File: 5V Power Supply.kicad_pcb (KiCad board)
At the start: 2 copper layers, 28.3 x 18 mm, 17 parts, among them Q1 CSD13202Q2, U1 TPS61287RZPR

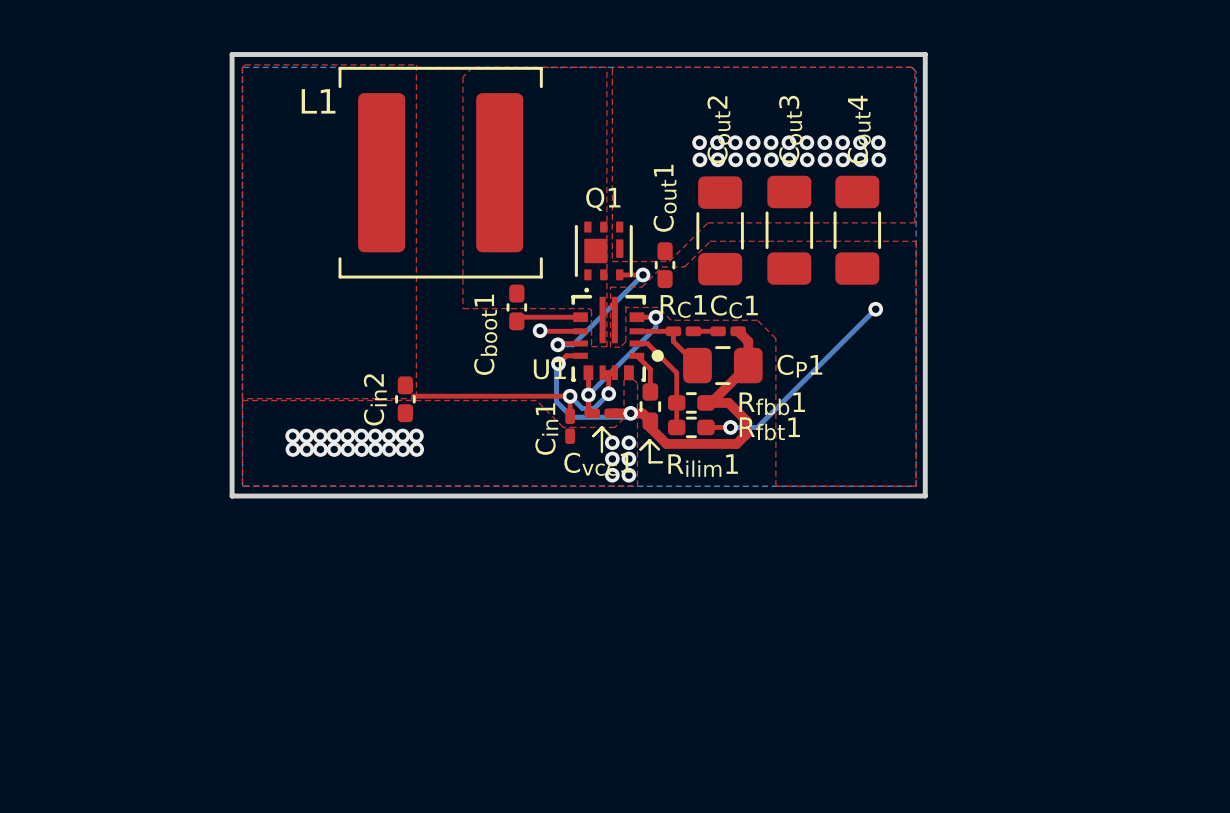
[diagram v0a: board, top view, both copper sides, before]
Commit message: feat: Mounting holes, power connectors
Added 2.54 mm ID mounting holes and 4 power connectors. Phoenix Contact spring loaded, good to 16 A, 14-26 AWG wire. 1x on power input from batt, 3x on +5V output.
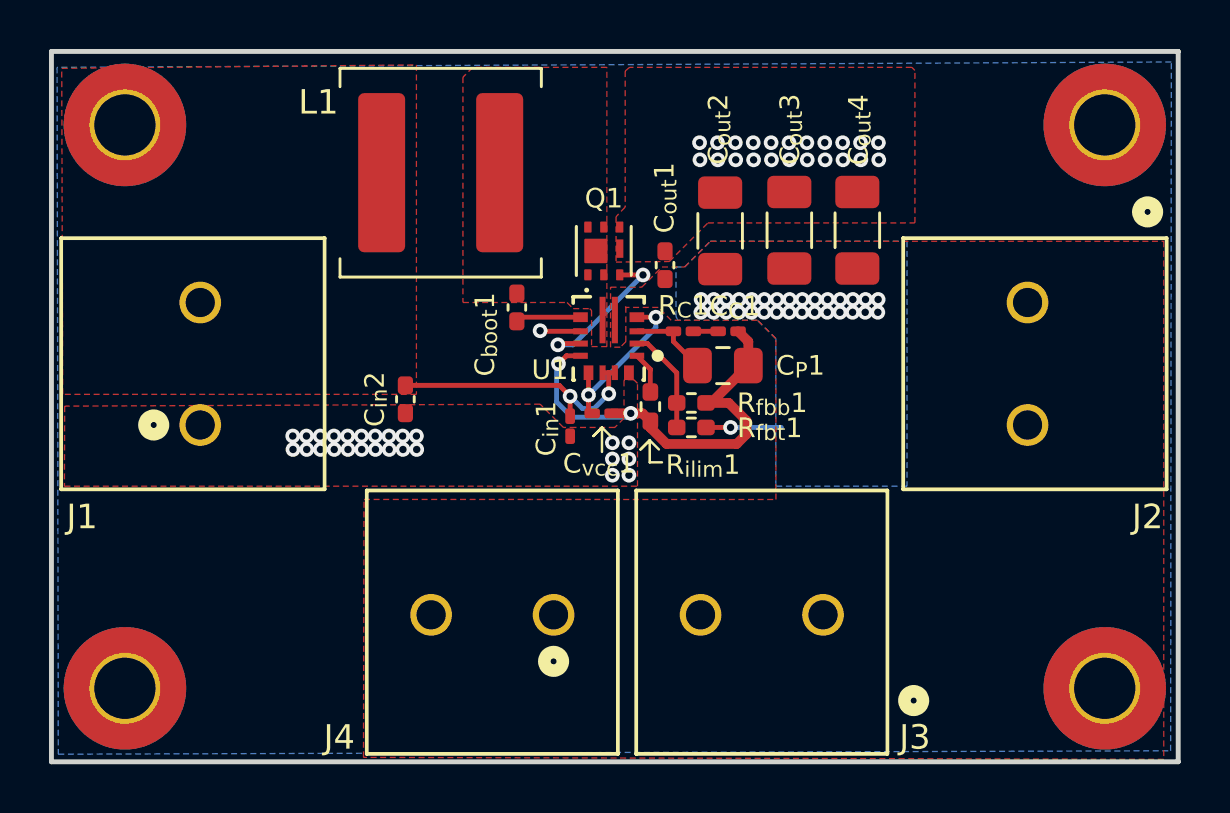
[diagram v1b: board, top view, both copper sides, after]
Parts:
- added J1: 1792863, 1792863:CONN_1792863_PXC, F.Cu at (60.1, 55.0)
- added J2: 1792863, 1792863:CONN_1792863_PXC, F.Cu at (93.8, 50.0)
- added J3: 1792863, 1792863:CONN_1792863_PXC, F.Cu at (85.5, 62.8)
- added J4: 1792863, 1792863:CONN_1792863_PXC, F.Cu at (74.5, 62.8)
- added REF**: MountingHole_2.5mm_Pad_TopBottom, MountingHole:MountingHole_2.5mm_Pad_TopBottom, F.Cu at (97.0, 65.8)
- added REF**: MountingHole_2.5mm_Pad_TopBottom, MountingHole:MountingHole_2.5mm_Pad_TopBottom, F.Cu at (97.0, 42.8)
- added REF**: MountingHole_2.5mm_Pad_TopBottom, MountingHole:MountingHole_2.5mm_Pad_TopBottom, F.Cu at (57.0, 65.8)
- added REF**: MountingHole_2.5mm_Pad_TopBottom, MountingHole:MountingHole_2.5mm_Pad_TopBottom, F.Cu at (57.0, 42.8)
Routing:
- net +5VDC: track 9.03 -> 3.08 mm, vias 2 -> 31
- net Vbat: track 10.6 -> 11.1 mm
- added copper zone on B.Cu, net +5VDC
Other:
- board size 28.3 x 18 mm -> 46 x 29 mm

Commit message: Added test points, silkscreening.
Need to consider input connector. Only rated to 16 A, but at lowest input voltage and highest output current need 18 A on input.
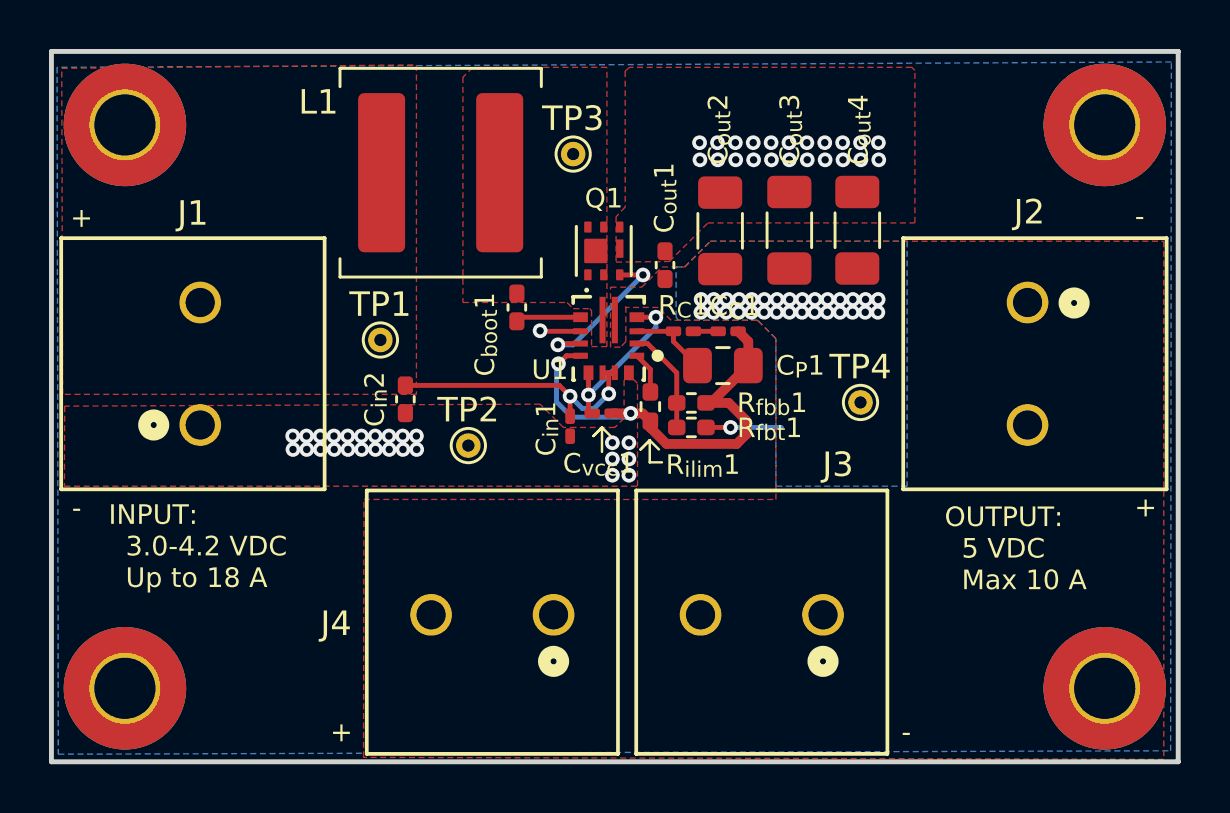
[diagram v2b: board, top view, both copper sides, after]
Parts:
- added TP1: TestPoint, TestPoint:TestPoint_THTPad_D1.0mm_Drill0.5mm, F.Cu at (67.4, 51.5)
- added TP2: TestPoint, TestPoint:TestPoint_THTPad_D1.0mm_Drill0.5mm, F.Cu at (71.0, 55.8)
- added TP3: TestPoint, TestPoint:TestPoint_THTPad_D1.0mm_Drill0.5mm, F.Cu at (75.3, 43.9)
- added TP4: TestPoint, TestPoint:TestPoint_THTPad_D1.0mm_Drill0.5mm, F.Cu at (87.0, 54.1)
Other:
- board text added: "+"
- board text added: "-"
- board text added: "INPUT: 3.0-4.2 VDC Up to 18 A"
- board text added: "OUTPUT: 5 VDC Max 10 A"

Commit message: Updated footprints
* Some of the footprints didn't match the size of the part picked for this project.
* Two of the capacitors were swapped.
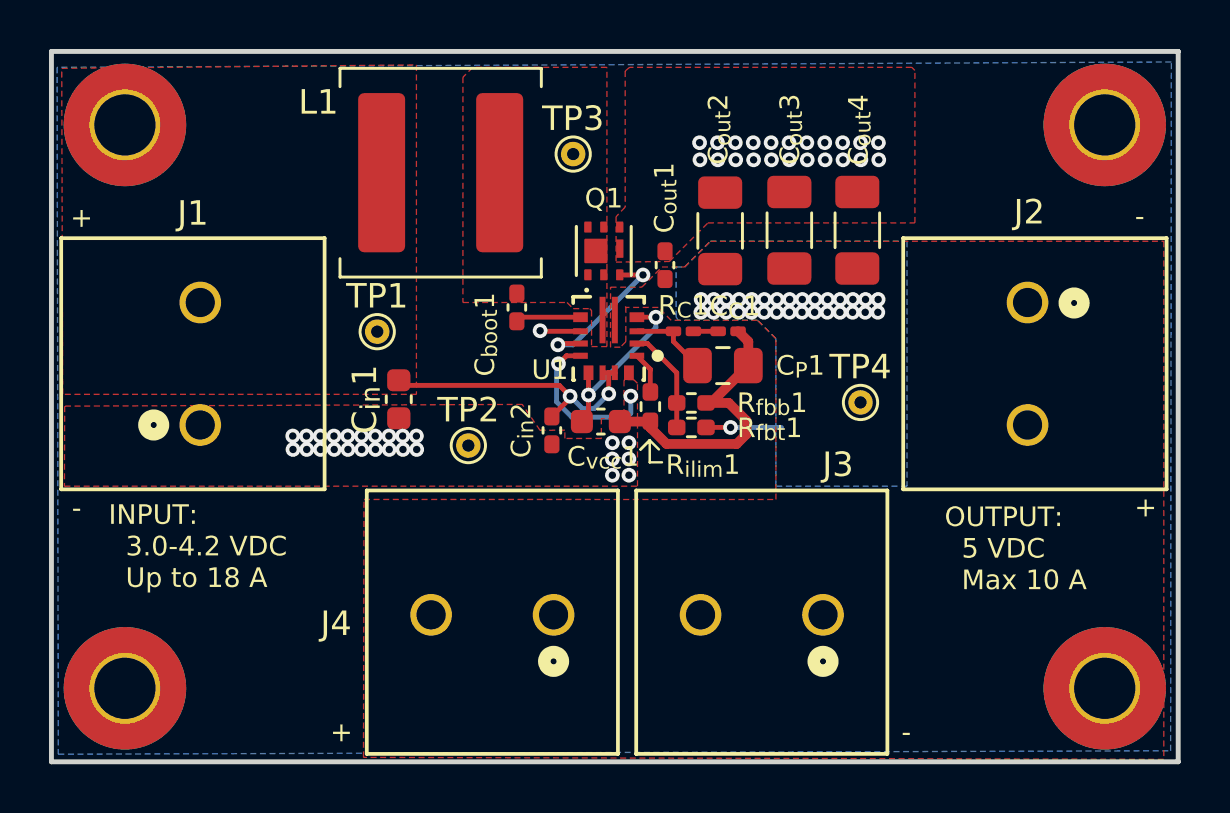
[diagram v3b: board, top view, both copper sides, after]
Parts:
- C_{in}1, C_{vcc}1: footprint Capacitor_SMD:C_0201_0603Metric_Pad0.64x0.40mm_HandSolder -> Capacitor_SMD:C_0603_1608Metric
- moved C_{in}1 7.08 mm to (68.2, 54.0)
- moved C_{in}2 6.11 mm to (74.4, 55.2)
- moved TP1 0.36 mm to (67.3, 51.2)
- moved C_{vcc}1 0.34 mm to (76.4, 54.9)

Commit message: feat: Modifications for v1.0
* Removed vias on input GND
* Added test points for measuring voltages. Added in pairs, with 2.5 mm spacing for O-scope spring ground probe
* Removed +5VDC ground pour on bottom layer
* Replaced the two 0201 components with 0402 components
* Adjusted some of the copper pour areas
* Adjusted/added silkscreening
* Moved J1 to get better positioning with top GND copper pour
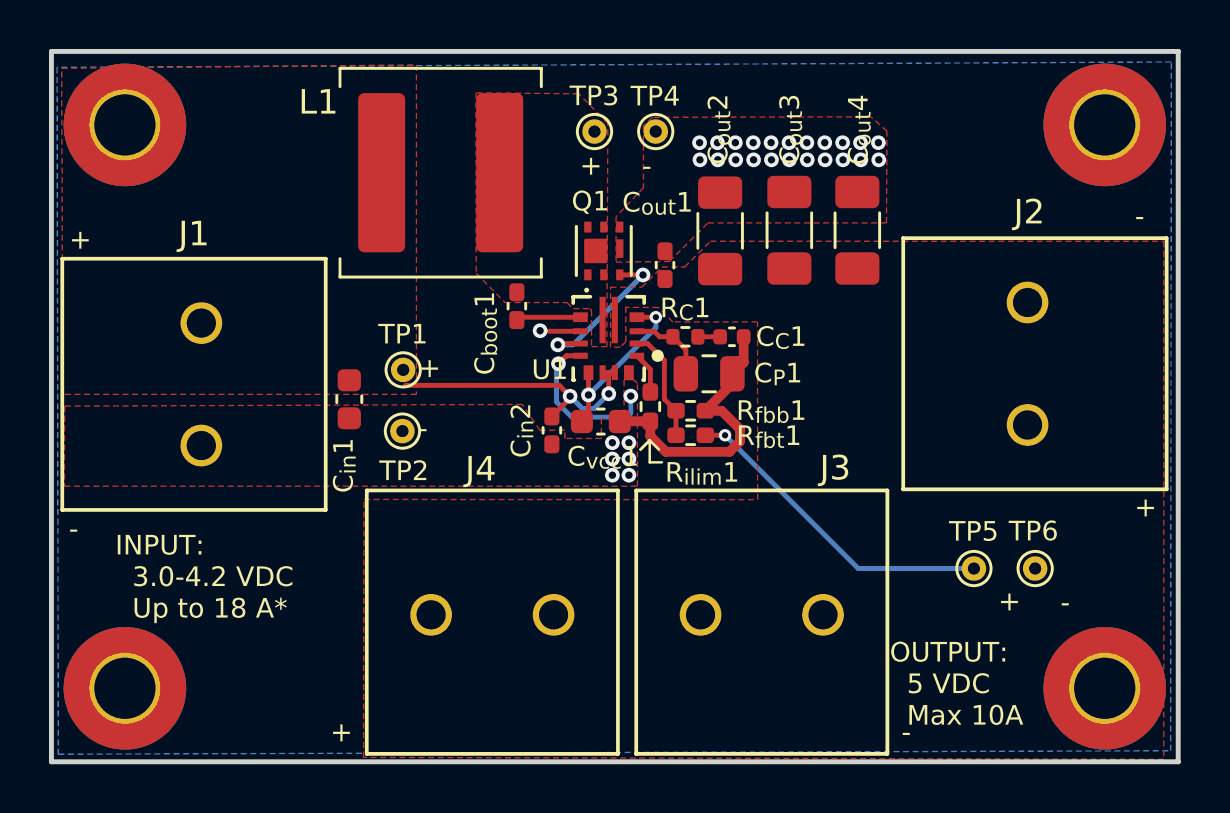
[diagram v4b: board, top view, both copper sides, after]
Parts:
- added TP5: TestPoint, TestPoint:TestPoint_THTPad_D1.0mm_Drill0.5mm, F.Cu at (91.7, 60.9)
- added TP6: TestPoint, TestPoint:TestPoint_THTPad_D1.0mm_Drill0.5mm, F.Cu at (94.2, 60.9)
- C_{C}1: footprint Capacitor_SMD:C_0201_0603Metric_Pad0.64x0.40mm_HandSolder -> Capacitor_SMD:C_0402_1005Metric
- C_{P}1: footprint Capacitor_SMD:C_0805_2012Metric_Pad1.18x1.45mm_HandSolder -> Capacitor_SMD:C_0805_2012Metric
- R_{C}1: footprint Resistor_SMD:R_0201_0603Metric_Pad0.64x0.40mm_HandSolder -> Resistor_SMD:R_0402_1005Metric
- moved TP4 13.9 mm to (78.7, 43.0)
- moved TP2 2.75 mm to (68.3, 55.2)
- moved C_{in}1 2.02 mm to (66.2, 54.0)
- moved TP1 1.89 mm to (68.4, 52.8)
- moved TP3 1.27 mm to (76.2, 43.0)
- moved J1 0.84 mm to (60.1, 55.8)
- moved C_{P}1 0.65 mm to (80.8, 52.9)
- moved R_{fbb}1 0.32 mm to (80.1, 54.4)
- moved R_{fbt}1 0.32 mm to (80.1, 55.4)
- moved C_{C}1 0.27 mm to (81.8, 51.4)
- moved R_{C}1 0.24 mm to (79.9, 51.4)
- moved C_{boot}1 0.05 mm to (73.0, 50.1)
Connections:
- TP4 pad 1: +5VDC -> GND
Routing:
- net +5VDC: track 3.08 -> 13.2 mm, vias 31 -> 1
- net GND: track 20.7 -> 20.2 mm, vias 51 -> 31
- removed copper zone on B.Cu, net +5VDC
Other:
- board text added: "*Phoenix Contact 1792863 is only rated to 16 A cont. At worst case, 10 A output with 3.0 V input, draw is 18 A. Limit output to 8.8 A if using this connector as input instead of hard-wire connection."
- board text added: "5V Power Supply v1.0 github.com/jseyfert3/5V-Power-Supply"
- board text added: "INPUT: 3.0-4.2 VDC Up to 18 A*"
- board text added: "OUTPUT: 5 VDC Max 10A"
- board text removed: "INPUT: 3.0-4.2 VDC Up to 18 A"
- board text removed: "OUTPUT: 5 VDC Max 10 A"
